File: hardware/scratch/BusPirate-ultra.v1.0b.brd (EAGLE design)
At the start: 100 x 50 mm, 167 parts, among them IC1 IC_MEM_23LC1024, IC10 IC_BUFF_SN74LVC1T45DBV, IC11 IC_BUFF_SN74LVC1T45DBV, IC12 74LVC1G07DBV, IC13 IC_BUFF_SN74LVC1T45DBV, IC17 74LVC1G07DBV, IC18 IC_BUFF_SN74LVC1T45DBV, IC19 74LVC1G07DBV, IC2 IC_MEM_23LC1024, IC20 IC_BUFF_SN74LVC1T45DBV, IC21 74LVC1G07DBV, IC22 IC_BUFF_SN74LVC1T45DBV, IC23 MCP1824_ADJ, IC24 74HCT4051, IC3 IC_74AC573, IC4 74LVC1G07DBV, IC5 74LVC1G07DBV, IC6 74LVC1G07DBV, IC7 74LVC1G07DBV, IC8 SN74LVC1T45DBV, IC9 IC_BUFF_SN74LVC1T45DBV, J1 CON_HEADER_2X02-PTH, J2 CON_HEADER_1X04, J3 CON_HEADER_1X03-PTH, J4 CON_HEADER_1X10-RIGHT_ANGLED_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, Q1 DMMT3906W, U1 W25X40CL, U2 IC_UC_STM32F103ZX, U3 IC_FPGA_ICE40HX4K, U4 MCP6001, U5 MCP4442, U6 MCP4442

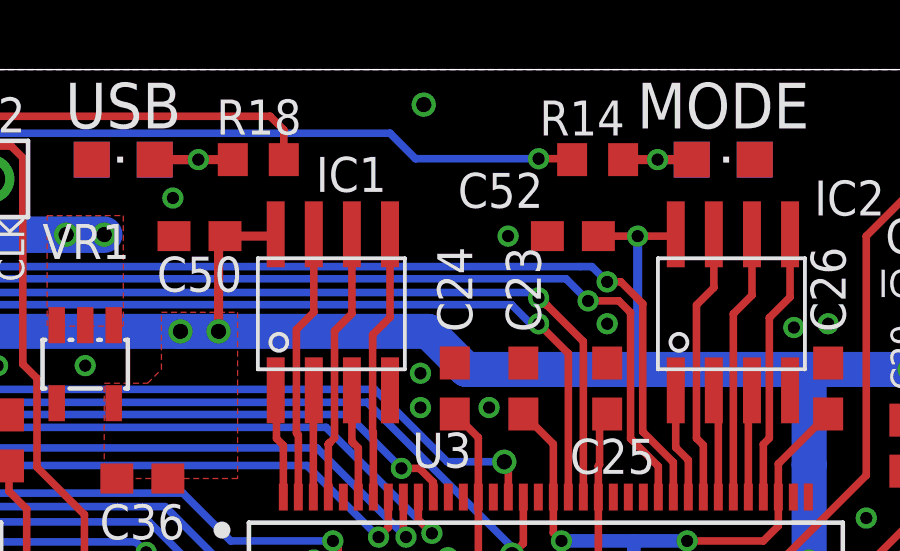
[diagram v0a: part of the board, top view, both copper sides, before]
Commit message: fix placement
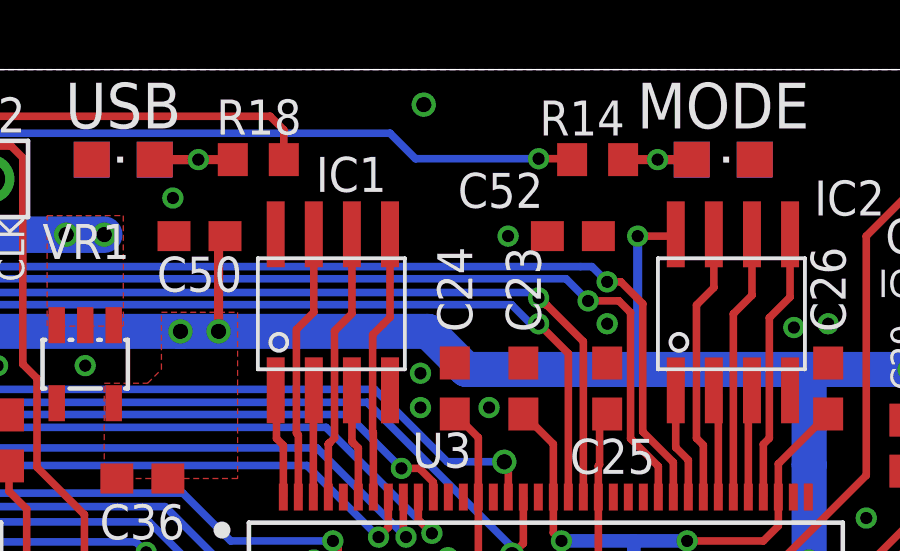
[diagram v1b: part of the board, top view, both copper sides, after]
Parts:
- IC10, IC11, IC13, IC18, IC20, IC22, IC9: value IC_BUFF_SN74LVC1T45DBV -> SN74LVC1T45DBV
- U2: value IC_UC_STM32F103ZX -> STM32F103ZX
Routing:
- net 3V3: track 513.8 -> 510.8 mm

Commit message: changes are.. -fix schematic placements -wired latch chip to BP IO and fix net names -SRAM chip CS pin connected to ARM chip -flipped connection of BP IO, MOSI now on pin 1, GND on pin 10... etc -removed reset button -removed boot mode jumper config pins -buffer Vb connected to Vref/Vout -UART pins changed to test pads -EEPROM pins breakout to pads -ADC/Analog mux control pins wired to FPGA
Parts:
- removed J1: CON_HEADER_2X02-PTH, dp_devices:M2X2
- removed J3: CON_HEADER_1X03-PTH, dp_devices.v6:M1X3
- removed SW1: (no value), dp_devices.v6:SW_TACT_SMALL
- added C51: 1uF, rcl:C0603
- added D1: (no value), dp_devices.v6:SOD-123
- added R50, R51: (no value), resistor:R0603
- added TP1, TP2, TP3, TP4, TP5, TP6, TP7, TP8: TPB1,27, testpad:B1,27
- added U7: MCP6001, dp_devices.v6:SOT-23-5
- IC1, IC2: value IC_MEM_23LC1024 -> 23LC1024
- IC3: value IC_74AC573 -> 74AC573
- U3: value IC_FPGA_ICE40HX4K -> ICE40HX4K
- moved C14 224.0 mm to (-10.8, -212.7)
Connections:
- net LAT_SWV33 renamed LAT_AUX2
- net LAT_SWV50 renamed LAT_AUX3
- removed net BPIO_AUX: IC3.7
- removed net LAT_CLK: IC3.17, U3.94
- removed net SWV33: IC3.8
- removed net SWV50: IC3.9
- removed net VEE: IC24.7
- removed net VPUN: C45.2, C46.2, C47.2, C48.2, C49.2, C56.2, C58.2, C60.2, IC10.6, IC11.6, IC13.6, IC18.6, IC20.6, IC22.6, IC8.6, IC9.6
- new net ADC_MUX_EN: IC24.6, U3.45
- new net FLASH_CS: TP7.TP, U1.1, U2.132
- new net LAT_CLOCK: IC3.18, U3.93
- new net N$64: R51.1, U7.1, U7.4
- new net N$65: R51.2, R9.1
- net 3V3: no longer J1.2, J1.4, U1.1
- net ADC_MUX_S0: now also U3.42
- net ADC_MUX_S1: now also U3.43
- net ADC_MUX_S2: now also U3.44
- net BOOT0: no longer J1.1
- net BOOT1: no longer J1.3
- net BPIO_AUX0: now also IC3.6, J4.5; no longer J4.6
- net BPIO_AUX1: now also IC3.7, J4.6; no longer J4.5
- net BPIO_AUX2: now also IC3.8, J4.7; no longer J4.4
- net BPIO_AUX3: now also IC3.9, J4.8; no longer J4.3
- net BPIO_CLOCK: now also IC3.3, J4.2; no longer IC3.4, J4.9
- net BPIO_CS: now also IC3.5, J4.4; no longer IC3.6, J4.7
- net BPIO_MISO: now also IC3.4, J4.3; no longer IC3.5, J4.8
- net BPIO_MOSI: now also IC3.2, J4.1; no longer IC3.3, J4.10
- net FLASH_MISO: now also TP5.TP
- net FLASH_MOSI: now also TP4.TP
- net FLASH_SCK: now also TP6.TP
- net GND: now also C14.2, C51.2, IC24.7, J4.10, TP1.TP, TP8.TP, U7.2; no longer C14.1, IC3.2, J3.1, J4.1, SW1.3, SW1.4
- net LAT_AUX0: now also IC3.15, U3.96; no longer IC3.14, U3.97
- net LAT_AUX1: now also IC3.14, U3.97; no longer IC3.19, U3.91
- net LAT_CS: now also IC3.16, U3.95; no longer IC3.15, U3.96
- net LAT_MISO: now also IC3.17, U3.94; no longer IC3.16, U3.95
- net LAT_MOSI: now also IC3.19, U3.91; no longer IC3.18, U3.93
- net N$32: now also D1.A, R50.2, U7.3; no longer IC24.3, R9.1
- net N$61: now also IC24.3, R50.1; no longer U2.132
- net RST: no longer C14.2, SW1.1, SW1.2
- net UART_RX: now also TP2.TP; no longer J3.2
- net UART_TX: now also TP3.TP; no longer J3.3
- net VREF/VOUT: now also C45.2, C46.2, C47.2, C48.2, C49.2, C56.2, C58.2, C60.2, IC10.6, IC11.6, IC13.6, IC18.6, IC20.6, IC22.6, IC8.6, IC9.6, J4.9; no longer J4.2
- net VUSB: now also C14.1, C51.1, D1.C, U7.5
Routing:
- net VREF/VOUT: track 0.00 -> 187.2 mm, vias 0 -> 12
- net VPUN: track 174.9 -> 0.00 mm, vias 12 -> 0
- net RST: track 83.0 -> 15.6 mm
- net BPIO_AUX1: track 0.00 -> 31.2 mm, vias 0 -> 1
- net BPIO_CLOCK: track 52.8 -> 28.0 mm
- net BPIO_MOSI: track 41.1 -> 20.2 mm
- net BPIO_MISO: track 43.4 -> 22.5 mm
- net BPIO_AUX0: track 20.2 -> 0.00 mm, vias 1 -> 0
- net BPIO_AUX3: track 0.00 -> 19.3 mm
- net BPIO_AUX2: track 0.00 -> 19.0 mm
- net GND: track 0.44 -> 19.3 mm
- net BPIO_CS: track 57.2 -> 40.0 mm
- net LAT_CLK: track 13.8 -> 0.00 mm
- net LAT_CLOCK: track 0.00 -> 12.6 mm
- net BPIO_AUX: track 11.0 -> 0.00 mm
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- added copper zone on layer 1, net BPIO_AUX2
- added copper zone on layer 1, net BPIO_AUX3
- added copper zone on layer 1, net VREF/VOUT
- removed copper zone on layer 1, net SWV33
- removed copper zone on layer 1, net SWV50
- removed copper zone on layer 1, net VPUN

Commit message: change BP IO to a more universal naming
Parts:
- moved R46 133.1 mm to (15.9, 6.99), turned to 90 degrees
- moved R47 132.9 mm to (17.8, 6.99), turned to 270 degrees
- moved R48 128.3 mm to (7.62, 6.99), turned to 270 degrees
- moved R49 123.4 mm to (8.89, 2.54), turned to 180 degrees
- moved C64 120.6 mm to (12.7, 5.08)
- moved C63 119.6 mm to (8.89, 3.81), turned to 180 degrees
- moved C61 118.5 mm to (17.1, 3.17), turned to 270 degrees
- moved R45 117.3 mm to (15.9, 3.17), turned to 90 degrees
- moved C62 113.7 mm to (9.53, 6.99), turned to 270 degrees
- moved U4 107.0 mm to (12.7, 6.99), turned to 90 degrees
- moved IC23 105.2 mm to (12.7, 3.17), turned to 270 degrees
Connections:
- net BPIO_AUX0 renamed BPIO4
- net BPIO_AUX1 renamed BPIO5
- net BPIO_AUX2 renamed BPIO6
- net BPIO_AUX3 renamed BPIO7
- net BPIO_CLOCK renamed BPIO1
- net BPIO_CS renamed BPIO3
- net BPIO_MISO renamed BPIO2
- net BPIO_MOSI renamed BPIO0
- net BUFDIR_AUX0 renamed BUFDIR4
- net BUFDIR_CLOCK renamed BUFDIR1
- net BUFDIR_CS renamed BUFDIR3
- net BUFDIR_MISO renamed BUFDIR2
- net BUFDIR_MOSI renamed BUFDIR0
- net BUFIO_AUX0 renamed BUFIO4
- net BUFIO_CLOCK renamed BUFIO1
- net BUFIO_CS renamed BUFIO3
- net BUFIO_MISO renamed BUFIO2
- net BUFIO_MOSI renamed BUFIO0
- net BUFOD_AUX0 renamed BUFOD4
- net BUFOD_CLOCK renamed BUFOD1
- net BUFOD_CS renamed BUFOD3
- net BUFOD_MISO renamed BUFOD2
- net BUFOD_MOSI renamed BUFOD0
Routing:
- net VREF/VOUT: track 187.2 -> 166.2 mm
- net VUSB: track 147.0 -> 138.2 mm, vias 16 -> 15
- net BPIO6: track 19.0 -> 13.1 mm
- net V50PU: track 25.7 -> 24.5 mm
- net GND: vias 146 -> 143
- removed copper zone on layer 1, net BPIO6
- removed copper zone on layer 1, net BPIO7
- removed copper zone on layer 1, net N$1
- removed copper zone on layer 1, net VEXTERN
- removed copper zone on layer 1, net VREF/VOUT

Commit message: route new vreg circuit
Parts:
- moved U6 176.9 mm to (71.1, 4.45), turned to 90 degrees
- moved U5 160.5 mm to (79.4, 4.45), turned to 90 degrees
- moved R43 138.2 mm to (20.1, 10.3), turned to 180 degrees
- moved R44 135.8 mm to (23.5, 8.13), turned to 270 degrees
- moved Q1 118.7 mm to (21.1, 8.13), turned to 180 degrees
- moved Q2 113.5 mm to (21.1, 3.94), turned to 90 degrees
- moved R48 6.20 mm to (12.7, 10.5), turned to 0 degrees
- moved C64 4.44 mm to (8.89, 7.37), turned to 180 degrees
- moved R12 4.07 mm to (4.45, 12.7), turned to 270 degrees
- moved C6 3.07 mm to (20.1, 11.9), turned to 180 degrees
- moved C62 1.89 mm to (8.89, 8.76), turned to 180 degrees
- moved R5 1.42 mm to (16.8, 11.8)
- moved C61 0.90 mm to (17.8, 3.81)
- moved U4 0.76 mm to (12.7, 7.75)
- moved IC23 0.64 mm to (12.7, 3.81)
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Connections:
- net !SHDN renamed VREG_EN
- new net VREG_PWM: R48.2
- net PWM: no longer R48.2
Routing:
- net VEXTPU: track 63.6 -> 0.00 mm, vias 3 -> 0
- net VUSB: track 138.2 -> 94.2 mm, vias 15 -> 13
- net N$12: track 0.00 -> 10.4 mm, vias 0 -> 2
- net N$26: track 0.00 -> 9.76 mm
- net VREF/VOUT: track 166.2 -> 173.5 mm, vias 12 -> 9
- net N$11: track 0.00 -> 7.25 mm, vias 0 -> 2
- net ADC6: track 6.37 -> 0.00 mm
- net ADC4: track 6.08 -> 0.00 mm
- net ADC2: track 6.02 -> 0.00 mm
- net ADC3: track 5.86 -> 0.00 mm
- net RST: track 15.6 -> 11.3 mm
- net N$15: track 0.00 -> 3.87 mm
- net N$25: track 0.00 -> 3.72 mm
- net N$27: track 0.00 -> 3.61 mm
- net VREGEN: track 86.7 -> 84.1 mm
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
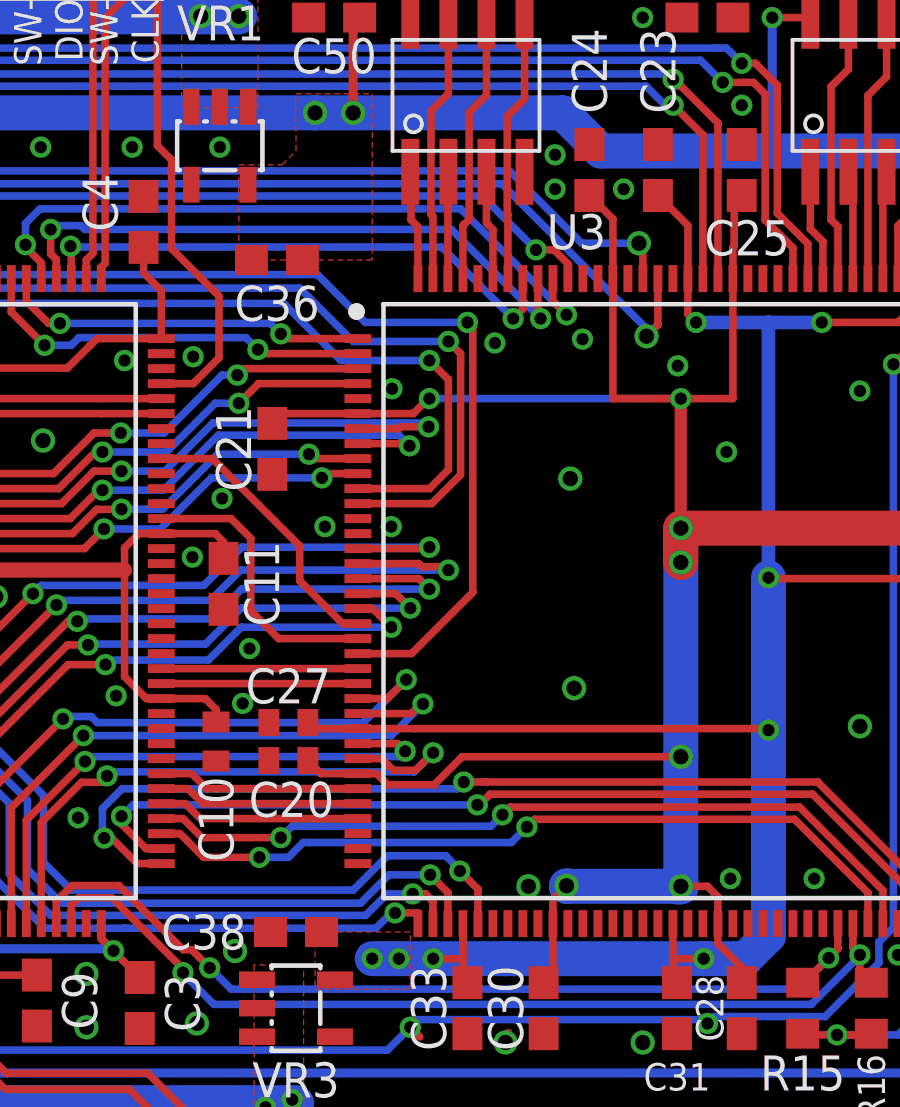
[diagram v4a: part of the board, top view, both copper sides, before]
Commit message: move things around, move MCU_INT1 to GBIN5 and MCU_MCO to GBIN1, fix VREGEN and VREG_EN
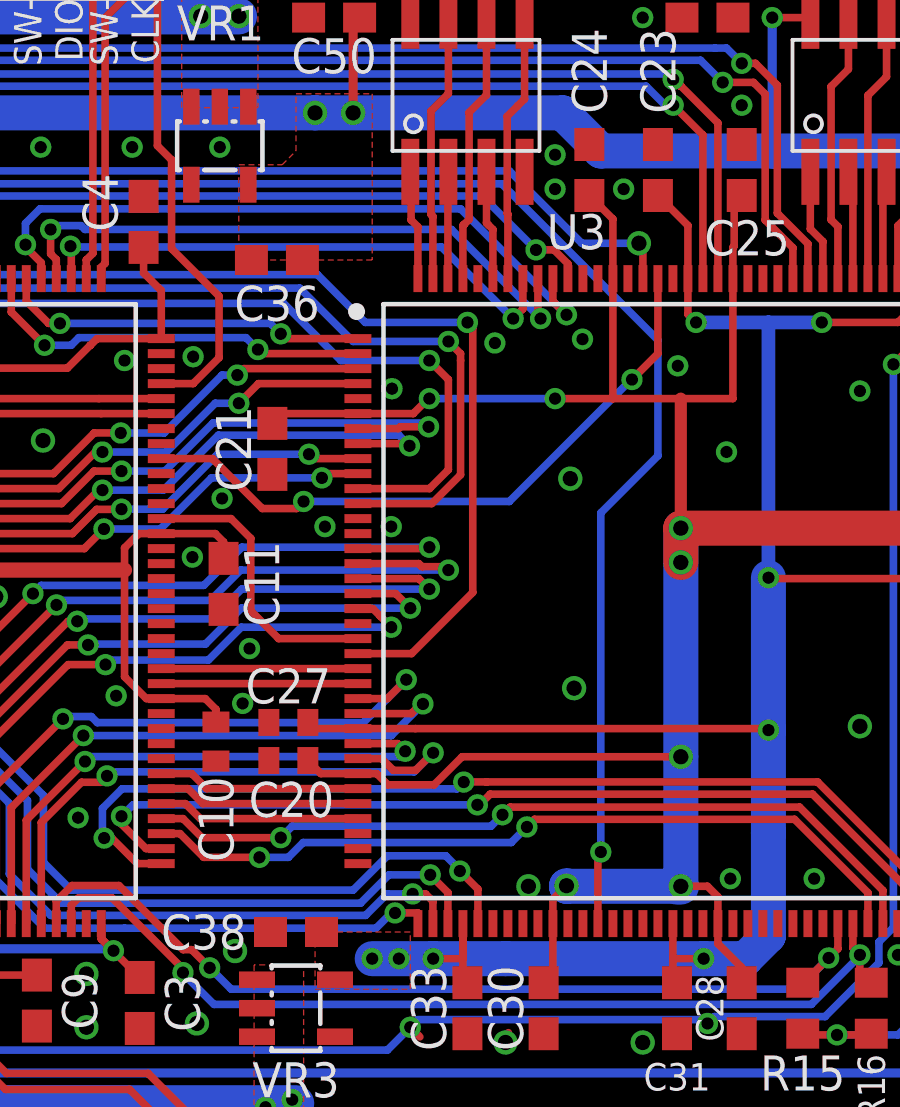
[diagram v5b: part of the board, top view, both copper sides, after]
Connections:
- removed net VREG_EN: IC23.3, R49.1
- net MCU_INT1: now also U3.49; no longer U3.128
- net MCU_MCO: now also U3.128; no longer U3.20
- net VREGEN: now also IC23.3, R49.1
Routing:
- net MCU_INT1: track 45.4 -> 63.9 mm
- net MCU_MCO: track 9.51 -> 21.9 mm, vias 0 -> 2
- net 3V3: track 503.9 -> 501.6 mm
- net VREG_EN: track 1.69 -> 0.00 mm
- net VREGEN: track 84.1 -> 85.8 mm
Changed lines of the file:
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@@
 <?xml version="1.0" encoding="utf-8"?>
 <!DOCTYPE eagle SYSTEM "eagle.dtd">
-<eagle version="9.4.2">
+<eagle version="9.1.3">
 <drawing>
 <settings>
@@
 <wire x1="-7.94" y1="-19.705" x2="-8.89" y2="-27.96" width="0" layer="19" extent="1-1"/>
 <wire x1="8.48995" y1="1.079875" x2="-7.94" y2="-19.705" width="0" layer="19" extent="1-1"/>
+<wire x1="40.4876" y1="29.2236" x2="38.8112" y2="28.4226" width="0" layer="19" extent="1-1"/>
 <wire x1="0.175" y1="20.315" x2="3.57505" y2="18.859875" width="0" layer="19" extent="1-1"/>
 <wire x1="0.175" y1="29.215" x2="3.57505" y2="31.13125" width="0" layer="19" extent="1-1"/>
@@
 <wire x1="64.04" y1="29.75" x2="62.865" y2="28.575" width="0.254" layer="1"/>
 <wire x1="54.102" y1="27.432" x2="54.102" y2="31.75" width="0.4064" layer="1"/>
-<wire x1="45.72" y1="31.75" x2="54.102" y2="31.75" width="0.254" layer="16"/>
-<via x="54.102" y="31.75" extent="1-16" drill="0.4064"/>
+<wire x1="45.72" y1="31.75" x2="49.911" y2="31.75" width="0.254" layer="16"/>
 <wire x1="50.292" y1="15.5128" x2="50.292" y2="15.494" width="1.1684" layer="16"/>
 <wire x1="50.292" y1="15.494" x2="53.975" y2="15.494" width="1.1684" layer="16"/>
@@
 <wire x1="18.285" y1="12.821" x2="19.216" y2="11.89" width="0.254" layer="1"/>
 <wire x1="18.285" y1="14.25" x2="18.285" y2="12.821" width="0.254" layer="1"/>
+<via x="49.911" y="31.75" extent="1-16" drill="0.4064"/>
+<wire x1="49.911" y1="31.75" x2="51.8393" y2="31.75" width="0.254" layer="1"/>
 <wire x1="-11.645" y1="-163.195" x2="-11.645" y2="-168.275" width="0" layer="19" extent="1-1"/>
 <wire x1="-11.645" y1="-147.955" x2="-11.645" y2="-163.195" width="0" layer="19" extent="1-1"/>
@@
 <wire x1="67.32" y1="47" x2="74.775" y2="47" width="0.254" layer="1"/>
 <wire x1="64.77" y1="44.45" x2="67.32" y2="47" width="0.254" layer="1"/>
+<contactref element="IC23" pad="3"/>
+<contactref element="R49" pad="1"/>
+<wire x1="11.4" y1="2.86" x2="9.806" y2="2.86" width="0.3048" layer="1"/>
+<wire x1="9.806" y1="2.86" x2="9.74" y2="2.794" width="0.3048" layer="1"/>
 <wire x1="44.323" y1="10.033" x2="44.265" y2="7.65" width="0" layer="19" extent="1-16"/>
+<wire x1="11.4" y1="2.86" x2="25.7984" y2="12.9366" width="0" layer="19" extent="1-1"/>
 </signal>
 <signal name="N$18">
@@
 </signal>
 <signal name="MCU_INT1">
-<contactref element="U3" pad="128"/>
 <via x="25.654" y="33.909" extent="1-16" drill="0.4064"/>
 <wire x1="28.8167375" y1="38.91" x2="48.133" y2="38.91" width="0.254" layer="16"/>
-<via x="52.959" y="33.83" extent="1-16" drill="0.508"/>
-<wire x1="53.3393" y1="34.206903125" x2="52.959" y2="33.83" width="0.254" layer="1"/>
-<wire x1="53.3393" y1="34.206903125" x2="53.3393" y2="35.75" width="0.254" layer="1"/>
 <contactref element="U2" pad="2"/>
 <wire x1="15.285" y1="33.25" x2="24.995" y2="33.25" width="0.254" layer="1"/>
 <wire x1="28.8167375" y1="38.91" x2="25.654" y2="35.7472625" width="0.254" layer="16"/>
-<wire x1="48.133" y1="38.91" x2="52.959" y2="34.084" width="0.254" layer="16"/>
-<wire x1="52.959" y1="34.084" x2="52.959" y2="33.83" width="0.254" layer="16"/>
 <wire x1="24.995" y1="33.25" x2="25.654" y2="33.909" width="0.254" layer="1"/>
 <wire x1="25.654" y1="35.7472625" x2="25.654" y2="33.909" width="0.254" layer="16"/>
+<wire x1="53.34" y1="29.845" x2="51.435" y2="27.94" width="0.254" layer="16"/>
+<wire x1="48.133" y1="38.91" x2="53.34" y2="33.703" width="0.254" layer="16"/>
+<wire x1="53.34" y1="33.703" x2="53.34" y2="29.845" width="0.254" layer="16"/>
+<contactref element="U3" pad="49"/>
+<wire x1="51.3393" y1="14.25" x2="51.3393" y2="16.5413" width="0.254" layer="1"/>
+<wire x1="51.3393" y1="16.5413" x2="51.435" y2="16.637" width="0.254" layer="1"/>
+<via x="51.435" y="16.637" extent="1-16" drill="0.4064"/>
+<wire x1="51.435" y1="16.637" x2="51.435" y2="27.94" width="0.254" layer="16"/>
 </signal>
 <signal name="PWM">
@@
 <signal name="MCU_MCO">
 <contactref element="U2" pad="100"/>
-<contactref element="U3" pad="20"/>
-<wire x1="38.4868" y1="29.75" x2="41.402" y2="26.8348" width="0.254" layer="1"/>
-<wire x1="41.402" y1="26.8348" x2="41.402" y2="25.6766" width="0.254" layer="1"/>
-<wire x1="41.402" y1="25.6766" x2="42.8286" y2="24.25" width="0.254" layer="1"/>
-<wire x1="42.8286" y1="24.25" x2="43.3393" y2="24.25" width="0.254" layer="1"/>
+<wire x1="38.4868" y1="29.75" x2="40.1509" y2="28.0859" width="0.254" layer="1"/>
 <wire x1="36.785" y1="29.75" x2="38.4868" y2="29.75" width="0.254" layer="1"/>
+<contactref element="U3" pad="128"/>
+<wire x1="40.1509" y1="28.0859" x2="41.2939" y2="28.0859" width="0.254" layer="1"/>
+<wire x1="41.2939" y1="28.0859" x2="41.529" y2="28.321" width="0.254" layer="1"/>
+<via x="41.529" y="28.321" extent="1-16" drill="0.4064"/>
+<wire x1="41.529" y1="28.321" x2="48.387" y2="28.321" width="0.254" layer="16"/>
+<wire x1="48.387" y1="28.321" x2="52.451" y2="32.385" width="0.254" layer="16"/>
+<via x="52.4743" y="32.385" extent="1-16" drill="0.4064"/>
+<wire x1="52.4743" y1="32.385" x2="53.3393" y2="33.25" width="0.254" layer="1"/>
+<wire x1="53.3393" y1="33.25" x2="53.3393" y2="35.75" width="0.254" layer="1"/>
+<wire x1="52.451" y1="32.385" x2="52.4743" y2="32.385" width="0.254" layer="16"/>
 </signal>
 <signal name="MCU_AUX6">
@@
 <wire x1="20.332" y1="9.028" x2="21.082" y2="9.028" width="0.4064" layer="1"/>
 </signal>
-<signal name="VREG_EN">
-<contactref element="IC23" pad="3"/>
-<contactref element="R49" pad="1"/>
-<wire x1="11.4" y1="2.86" x2="9.806" y2="2.86" width="0.3048" layer="1"/>
-<wire x1="9.806" y1="2.86" x2="9.74" y2="2.794" width="0.3048" layer="1"/>
-</signal>
 <signal name="BPIO5">
